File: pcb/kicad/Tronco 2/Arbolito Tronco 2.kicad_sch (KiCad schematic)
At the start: 14 parts, among them J1 Conn_01x01, J2 Conn_01x01, J3 Conn_01x01, J4 Conn_01x01, J5 Conn_01x01, J6 Conn_01x01, U1 WS2812B, U2 WS2812B, U3 WS2812B, U4 WS2812B

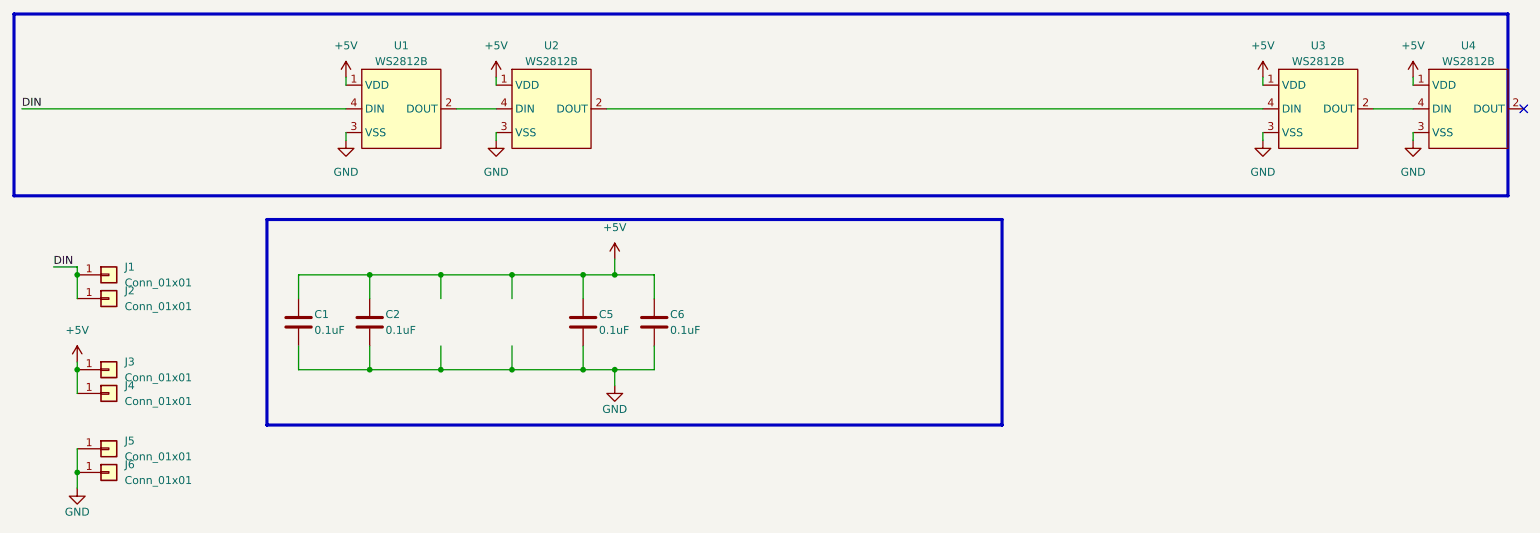
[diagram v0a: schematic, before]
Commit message: Added Rev3 release files
- Added ibom html files
- Update ibom in .web directory
- Update pdf schematics
- Added 3D steps files
- Added tools for help to mount the PCB
- Added hw rev3 gerber files
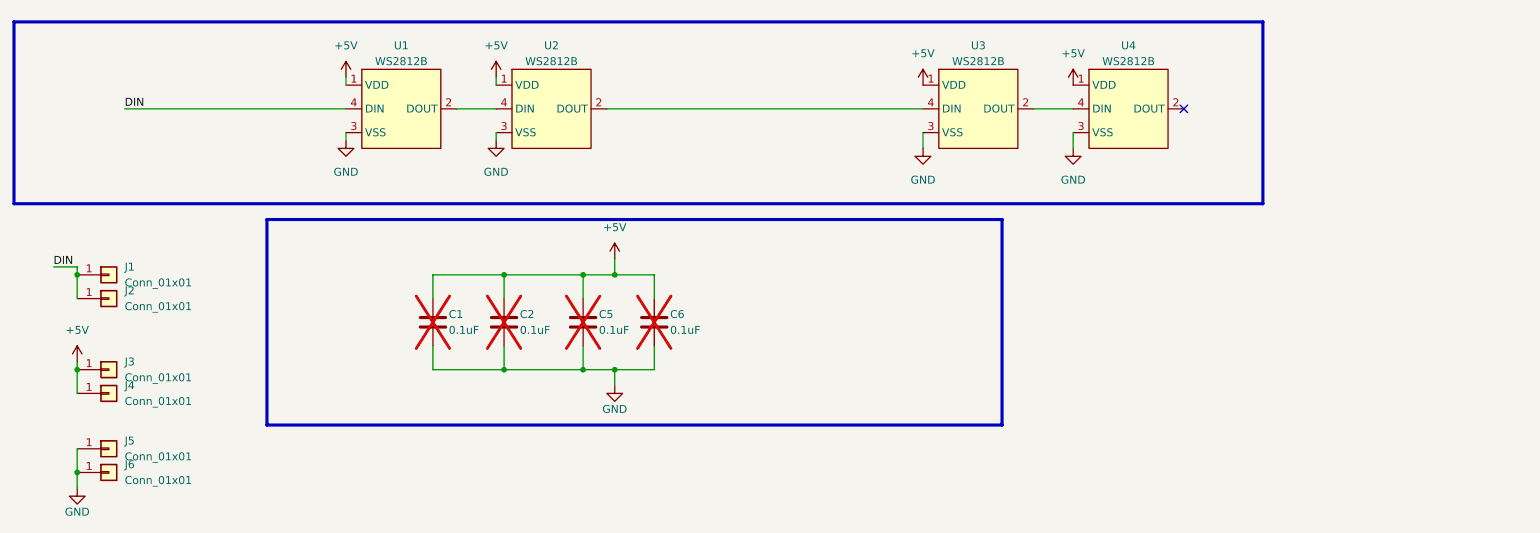
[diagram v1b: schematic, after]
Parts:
- C1, C2, C5, C6: now not fitted
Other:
- moved on the sheet: U3, U4
